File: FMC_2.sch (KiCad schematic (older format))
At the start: 16 parts, among them P2 SAMTEC_ASP-134603-01

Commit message: Get rid of most .DbLib suffixes in Library Name attributes
Enough that KiBoM no longer complains about them
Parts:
- R299, R300: Library Name Resistors.DbLib -> Resistors SMD
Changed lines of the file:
@@
 F 37 "10/17/12 00:00:00" H 3100 2430 50  0001 L CNN "LatestRevisionDate"
 F 38 "Resistors SMD" H 3100 2355 50  0001 L CNN "Database Table Name"
-F 39 "Resistors.DbLib" H 3100 2280 50  0001 L CNN "Library Name"
+F 39 "Resistors SMD" H 3100 2280 50  0001 L CNN "Library Name"
 F 40 "Resistors SMD" H 3100 2205 50  0001 L CNN "Footprint Library"
 F 41 "This work is licensed under the Creative Commons CC-BY-SA 4.0 License. To the extent that circuit schematics that use Licensed Material can be considered to be ‘Adapted Material’, then the copyright holder waives article 3.b of the license with respect to these schematics." H 3100 2130 50  0001 L CNN "License"
@@
 F 37 "10/17/12 00:00:00" H 5150 2530 50  0001 L CNN "LatestRevisionDate"
 F 38 "Resistors SMD" H 5150 2455 50  0001 L CNN "Database Table Name"
-F 39 "Resistors.DbLib" H 5150 2380 50  0001 L CNN "Library Name"
+F 39 "Resistors SMD" H 5150 2380 50  0001 L CNN "Library Name"
 F 40 "Resistors SMD" H 5150 2305 50  0001 L CNN "Footprint Library"
 F 41 "This work is licensed under the Creative Commons CC-BY-SA 4.0 License. To the extent that circuit schematics that use Licensed Material can be considered to be ‘Adapted Material’, then the copyright holder waives article 3.b of the license with respect to these schematics." H 5150 2230 50  0001 L CNN "License"

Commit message: Get rid of more useless inconsistencies in Comment attributes
Makes for quieter KiBoM runs
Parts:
- R299, R300: Comment 240 -> =Value
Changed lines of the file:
@@
 F 6 "Resistor - 1%" H 3100 4755 50  0001 L CNN "Library Ref"
 F 7 "SchLib\\Resistors.SchLib" H 3100 4680 50  0001 L CNN "Library Path"
-F 8 "240" H 3100 4605 50  0001 L CNN "Comment"
+F 8 "=Value" H 3100 4605 50  0001 L CNN "Comment"
 F 9 "Standard" H 3100 4530 50  0001 L CNN "Component Kind"
 F 10 "Standard" H 3100 4455 50  0001 L CNN "Component Type"
@@
 F 6 "Resistor - 1%" H 5150 4855 50  0001 L CNN "Library Ref"
 F 7 "SchLib\\Resistors.SchLib" H 5150 4780 50  0001 L CNN "Library Path"
-F 8 "240" H 5150 4705 50  0001 L CNN "Comment"
+F 8 "=Value" H 5150 4705 50  0001 L CNN "Comment"
 F 9 "Standard" H 5150 4630 50  0001 L CNN "Component Kind"
 F 10 "Standard" H 5150 4555 50  0001 L CNN "Component Type"

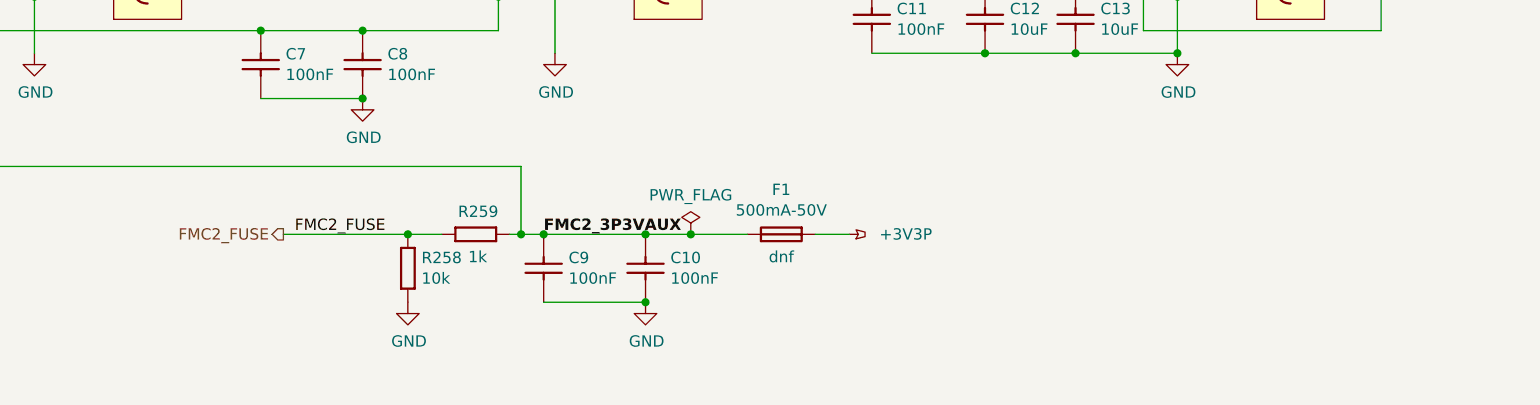
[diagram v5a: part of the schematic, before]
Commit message: added MIC2090-1
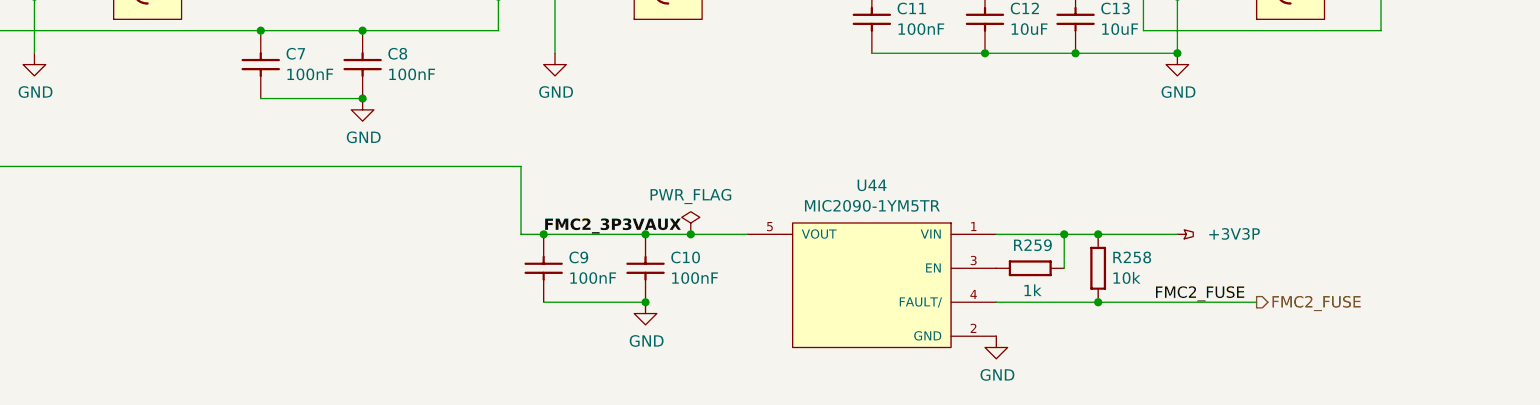
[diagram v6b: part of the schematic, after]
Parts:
- removed F1: FUS0603_BOURNS-SF-0603F050-2, Marble:FUSC1608X55N, symbol Fuses:FUS0603_BOURNS-SF-0603F050-2
- added U44: MIC2090-1YM5TR, ICs And Semiconductors SMD:SOT95P280X145-5N, symbol Analog_&_Interface:MIC2090-1YM5TR
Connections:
- net +3V3P: now also R258.1, R259.1, U44.1 (VIN)
- net FMC2_3P3VAUX: now also U44.5 (VOUT); no longer R259.1
- net FMC2_FUSE: now also R258.2, U44.4 (FAULT/); no longer R258.1, R259.2
- net GND: now also U44.2 (GND); no longer R258.2
- new net: R259.2, U44.3 (EN)
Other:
- moved on the sheet: R258, R259

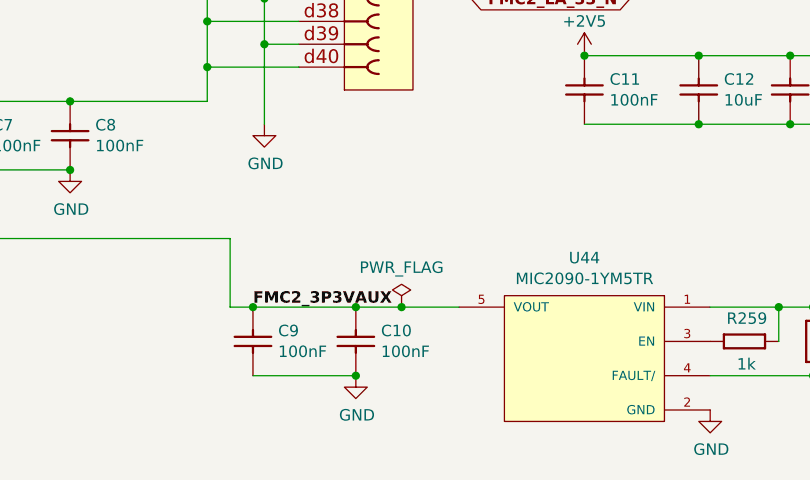
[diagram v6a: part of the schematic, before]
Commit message: remove power flag at U44, U45 VOUT-pin
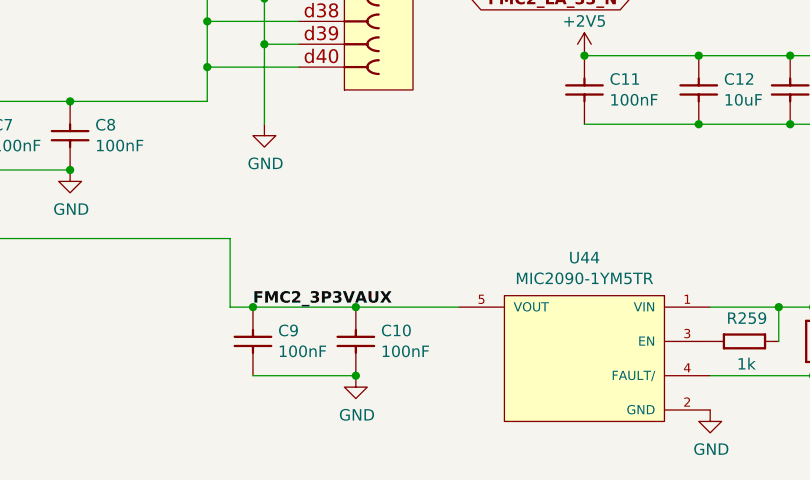
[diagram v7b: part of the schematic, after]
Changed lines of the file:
@@
 	5950 6900 6400 6900
 Connection ~ 6400 6900
-Wire Wire Line
-	6400 6900 6600 6900
 Connection ~ 6400 7200
 Wire Wire Line
@@
 	7900 5800 8300 5800
 $Comp
-L power:PWR_FLAG #FLG0118
-U 1 1 5EC3D861
-P 6600 6900
-F 0 "#FLG0118" H 6600 6975 50  0001 C CNN
-F 1 "PWR_FLAG" H 6600 7073 50  0000 C CNN
-F 2 "" H 6600 6900 50  0001 C CNN
-F 3 "" H 6600 6900 50  0001 C CNN
-	1    6600 6900
-	1    0    0    -1
-$EndComp
-$Comp
 L Resistors_SMD:R0402_240R_1%_0.0625W_100PPM R299
 U 1 1 5ED979B2
@@
 Wire Wire Line
 	5850 6900 5950 6900
-Connection ~ 6600 6900
-Wire Wire Line
-	6600 6900 6850 6900
 $Comp
 L power:+3V3P #PWR?
@@
 	8400 7200 7950 7200
 Connection ~ 8400 7200
+Wire Wire Line
+	6400 6900 6850 6900
 $EndSCHEMATC

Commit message: Get rid of "~" attribute in instances
This makes instances line up better with our library
Use a very short python program to rename "~" to "Val" and remove the old "Val".
Required a little pre-patch to correctly handle R297 R298 R299 R300 R162 R274 R197 R198, which had no "~" field.
No net changes to "Val" field contents.
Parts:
- C10, C11, C5, C7, C8, C9: ~ 100nF -> (none)
- C12, C13, C6: ~ 10uF -> (none)
- R205, R258: ~ 10k -> (none)
- R259: ~ 1k -> (none)
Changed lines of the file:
@@
 F 2 "Marble:RESC1005X40N" H 10650 480 60  0001 L CNN
 F 3 "\\\\cern.ch\\dfs\\Applications\\Altium\\Datasheets\\R0402_Phycomp_RC0402.pdf" H 10650 1110 60  0001 L CNN
-F 4 "10k" V 10845 1560 50  0000 L CNN "~"
+F 4 "10k" V 10845 1560 50  0000 L CNN "Val"
 F 5 "R0402_10K_1%_0.0625W_100PPM" H 10650 1020 60  0001 L CNN "Part Number"
 F 6 "Resistor - 1%" H 10650 930 60  0001 L CNN "Library Ref"
@@
 F 13 "PcbLib\\Resistors SMD.PcbLib" H 10650 210 60  0001 L CNN "Footprint Path"
 F 14 "RESC1005X40N" H 10650 120 60  0001 L CNN "Footprint Ref"
-F 15 "10k" H 10650 30  60  0001 L CNN "Val"
 F 16 "Not Recommended" H 10650 -60 60  0001 L CNN "Status"
 F 17 "0.0625W" H 10650 -150 60  0001 L CNN "Power"
@@
 F 2 "Marble:CAPC0603X33N" H 7400 4730 60  0001 L CNN
 F 3 "\\\\cern.ch\\dfs\\Applications\\Altium\\Datasheets\\CC0201_X5R_AVX.pdf" H 7400 5360 60  0001 L CNN
-F 4 "100nF" V 7595 5910 50  0000 L CNN "~"
+F 4 "100nF" V 7595 5910 50  0000 L CNN "Val"
 F 5 "CC0201_100NF_6.3V_10%_X5R" H 7400 5270 60  0001 L CNN "Part Number"
 F 6 "Capacitor - non polarized" H 7400 5180 60  0001 L CNN "Library Ref"
@@
 F 13 "CAPC0603X33N" H 7400 4460 60  0001 L CNN "Footprint Ref"
 F 14 "~~" H 7400 4370 60  0001 L CNN "PackageDescription"
-F 15 "100nF" H 7400 4280 60  0001 L CNN "Val"
 F 16 "Not Recommended" H 7400 4190 60  0001 L CNN "Status"
 F 17 "~~" H 7400 4100 60  0001 L CNN "Status Comment"
@@
 F 2 "Marble:CAPC3216X140N" H 3000 4280 60  0001 L CNN
 F 3 "\\\\cern.ch\\dfs\\Applications\\Altium\\Datasheets\\CC1206_X7R_KEMET.pdf" H 3000 4910 60  0001 L CNN
-F 4 "10uF" V 3195 5460 50  0000 L CNN "~"
+F 4 "10uF" V 3195 5460 50  0000 L CNN "Val"
 F 5 "CC1206_10UF_16V_10%_X7R" H 3000 4820 60  0001 L CNN "Part Number"
 F 6 "Capacitor - non polarized" H 3000 4730 60  0001 L CNN "Library Ref"
@@
 F 13 "CAPC3216X140N" H 3000 4010 60  0001 L CNN "Footprint Ref"
 F 14 "~~" H 3000 3920 60  0001 L CNN "PackageDescription"
-F 15 "10uF" H 3000 3830 60  0001 L CNN "Val"
 F 16 "Preferred" H 3000 3740 60  0001 L CNN "Status"
 F 17 "~~" H 3000 3650 60  0001 L CNN "Status Comment"
@@
 F 2 "Marble:CAPC0603X33N" H 4700 4930 60  0001 L CNN
 F 3 "\\\\cern.ch\\dfs\\Applications\\Altium\\Datasheets\\CC0201_X5R_AVX.pdf" H 4700 5560 60  0001 L CNN
-F 4 "100nF" V 4895 6110 50  0000 L CNN "~"
+F 4 "100nF" V 4895 6110 50  0000 L CNN "Val"
 F 5 "CC0201_100NF_6.3V_10%_X5R" H 4700 5470 60  0001 L CNN "Part Number"
 F 6 "Capacitor - non polarized" H 4700 5380 60  0001 L CNN "Library Ref"
@@
 F 13 "CAPC0603X33N" H 4700 4660 60  0001 L CNN "Footprint Ref"
 F 14 "~~" H 4700 4570 60  0001 L CNN "PackageDescription"
-F 15 "100nF" H 4700 4480 60  0001 L CNN "Val"
 F 16 "Not Recommended" H 4700 4390 60  0001 L CNN "Status"
 F 17 "~~" H 4700 4300 60  0001 L CNN "Status Comment"
@@
 F 2 "Marble:CAPC1608X87N" H 8300 5030 60  0001 L CNN
 F 3 "\\\\cern.ch\\dfs\\Applications\\Altium\\Datasheets\\CC0603_X5R_KEMET.pdf" H 8300 5660 60  0001 L CNN
-F 4 "10uF" V 8405 5990 50  0000 R CNN "~"
+F 4 "10uF" V 8405 5990 50  0000 R CNN "Val"
 F 5 "CC0603_10UF_6.3V_20%_X5R" H 8300 5570 60  0001 L CNN "Part Number"
 F 6 "Capacitor - non polarized" H 8300 5480 60  0001 L CNN "Library Ref"
@@
 F 13 "CAPC1608X87N" H 8300 4760 60  0001 L CNN "Footprint Ref"
 F 14 "~~" H 8300 4670 60  0001 L CNN "PackageDescription"
-F 15 "10uF" H 8300 4580 60  0001 L CNN "Val"
 F 16 "Preferred" H 8300 4490 60  0001 L CNN "Status"
 F 17 "~~" H 8300 4400 60  0001 L CNN "Status Comment"
@@
 F 2 "Marble:CAPC1005X55N" H 2500 4280 60  0001 L CNN
 F 3 "\\\\cern.ch\\dfs\\Applications\\Altium\\Datasheets\\CC0402_X5R_MURATA_GRM.pdf" H 2500 4910 60  0001 L CNN
-F 4 "100nF" V 2750 5350 50  0000 L CNN "~"
+F 4 "100nF" V 2750 5350 50  0000 L CNN "Val"
 F 5 "CC0402_100NF_16V_10%_X5R" H 2500 4820 60  0001 L CNN "Part Number"
 F 6 "Capacitor - non polarized" H 2500 4730 60  0001 L CNN "Library Ref"
@@
 F 13 "CAPC1005X55N" H 2500 4010 60  0001 L CNN "Footprint Ref"
 F 14 "~~" H 2500 3920 60  0001 L CNN "PackageDescription"
-F 15 "100nF" H 2500 3830 60  0001 L CNN "Val"
 F 16 "None" H 2500 3740 60  0001 L CNN "Status"
 F 17 "~~" H 2500 3650 60  0001 L CNN "Status Comment"
@@
 F 2 "Marble:RESC1005X40N" H 8400 5880 60  0001 L CNN
 F 3 "\\\\cern.ch\\dfs\\Applications\\Altium\\Datasheets\\R0402_Phycomp_RC0402.pdf" H 8400 6510 60  0001 L CNN
-F 4 "10k" V 8595 6960 50  0000 L CNN "~"
+F 4 "10k" V 8595 6960 50  0000 L CNN "Val"
 F 5 "R0402_10K_1%_0.0625W_100PPM" H 8400 6420 60  0001 L CNN "Part Number"
 F 6 "Resistor - 1%" H 8400 6330 60  0001 L CNN "Library Ref"
@@
 F 13 "PcbLib\\Resistors SMD.PcbLib" H 8400 5610 60  0001 L CNN "Footprint Path"
 F 14 "RESC1005X40N" H 8400 5520 60  0001 L CNN "Footprint Ref"
-F 15 "10k" H 8400 5430 60  0001 L CNN "Val"
 F 16 "Not Recommended" H 8400 5340 60  0001 L CNN "Status"
 F 17 "0.0625W" H 8400 5250 60  0001 L CNN "Power"
@@
 F 2 "Marble:RESC1005X40N" H 8250 6030 60  0001 L CNN
 F 3 "\\\\cern.ch\\dfs\\Applications\\Altium\\Datasheets\\R0402_Phycomp_RC0402.pdf" H 8250 6660 60  0001 L CNN
-F 4 "1k" H 8350 7150 50  0000 L CNN "~"
+F 4 "1k" H 8350 7150 50  0000 L CNN "Val"
 F 5 "R0402_1K_1%_0.0625W_100PPM" H 8250 6570 60  0001 L CNN "Part Number"
 F 6 "Resistor - 1%" H 8250 6480 60  0001 L CNN "Library Ref"
@@
 F 13 "PcbLib\\Resistors SMD.PcbLib" H 8250 5760 60  0001 L CNN "Footprint Path"
 F 14 "RESC1005X40N" H 8250 5670 60  0001 L CNN "Footprint Ref"
-F 15 "1k" H 8250 5580 60  0001 L CNN "Val"
 F 16 "Not Recommended" H 8250 5490 60  0001 L CNN "Status"
 F 17 "0.0625W" H 8250 5400 60  0001 L CNN "Power"
@@
 F 2 "Marble:CAPC0603X33N" H 5150 4930 60  0001 L CNN
 F 3 "\\\\cern.ch\\dfs\\Applications\\Altium\\Datasheets\\CC0201_X5R_AVX.pdf" H 5150 5560 60  0001 L CNN
-F 4 "100nF" V 5345 6110 50  0000 L CNN "~"
+F 4 "100nF" V 5345 6110 50  0000 L CNN "Val"
 F 5 "CC0201_100NF_6.3V_10%_X5R" H 5150 5470 60  0001 L CNN "Part Number"
 F 6 "Capacitor - non polarized" H 5150 5380 60  0001 L CNN "Library Ref"
@@
 F 13 "CAPC0603X33N" H 5150 4660 60  0001 L CNN "Footprint Ref"
 F 14 "~~" H 5150 4570 60  0001 L CNN "PackageDescription"
-F 15 "100nF" H 5150 4480 60  0001 L CNN "Val"
 F 16 "Not Recommended" H 5150 4390 60  0001 L CNN "Status"
 F 17 "~~" H 5150 4300 60  0001 L CNN "Status Comment"
@@
 F 2 "Marble:CAPC0603X33N" H 5950 5830 60  0001 L CNN
 F 3 "\\\\cern.ch\\dfs\\Applications\\Altium\\Datasheets\\CC0201_X5R_AVX.pdf" H 5950 6460 60  0001 L CNN
-F 4 "100nF" V 6145 7010 50  0000 L CNN "~"
+F 4 "100nF" V 6145 7010 50  0000 L CNN "Val"
 F 5 "CC0201_100NF_6.3V_10%_X5R" H 5950 6370 60  0001 L CNN "Part Number"
 F 6 "Capacitor - non polarized" H 5950 6280 60  0001 L CNN "Library Ref"
@@
 F 13 "CAPC0603X33N" H 5950 5560 60  0001 L CNN "Footprint Ref"
 F 14 "~~" H 5950 5470 60  0001 L CNN "PackageDescription"
-F 15 "100nF" H 5950 5380 60  0001 L CNN "Val"
 F 16 "Not Recommended" H 5950 5290 60  0001 L CNN "Status"
 F 17 "~~" H 5950 5200 60  0001 L CNN "Status Comment"
@@
 F 2 "Marble:CAPC0603X33N" H 6400 5830 60  0001 L CNN
 F 3 "\\\\cern.ch\\dfs\\Applications\\Altium\\Datasheets\\CC0201_X5R_AVX.pdf" H 6400 6460 60  0001 L CNN
-F 4 "100nF" V 6595 7010 50  0000 L CNN "~"
+F 4 "100nF" V 6595 7010 50  0000 L CNN "Val"
 F 5 "CC0201_100NF_6.3V_10%_X5R" H 6400 6370 60  0001 L CNN "Part Number"
 F 6 "Capacitor - non polarized" H 6400 6280 60  0001 L CNN "Library Ref"
@@
 F 13 "CAPC0603X33N" H 6400 5560 60  0001 L CNN "Footprint Ref"
 F 14 "~~" H 6400 5470 60  0001 L CNN "PackageDescription"
-F 15 "100nF" H 6400 5380 60  0001 L CNN "Val"
 F 16 "Not Recommended" H 6400 5290 60  0001 L CNN "Status"
 F 17 "~~" H 6400 5200 60  0001 L CNN "Status Comment"
@@
 F 2 "Marble:CAPC1608X87N" H 7900 5030 60  0001 L CNN
 F 3 "\\\\cern.ch\\dfs\\Applications\\Altium\\Datasheets\\CC0603_X5R_KEMET.pdf" H 7900 5660 60  0001 L CNN
-F 4 "10uF" V 8005 5990 50  0000 R CNN "~"
+F 4 "10uF" V 8005 5990 50  0000 R CNN "Val"
 F 5 "CC0603_10UF_6.3V_20%_X5R" H 7900 5570 60  0001 L CNN "Part Number"
 F 6 "Capacitor - non polarized" H 7900 5480 60  0001 L CNN "Library Ref"
@@
 F 13 "CAPC1608X87N" H 7900 4760 60  0001 L CNN "Footprint Ref"
 F 14 "~~" H 7900 4670 60  0001 L CNN "PackageDescription"
-F 15 "10uF" H 7900 4580 60  0001 L CNN "Val"
 F 16 "Preferred" H 7900 4490 60  0001 L CNN "Status"
 F 17 "~~" H 7900 4400 60  0001 L CNN "Status Comment"
